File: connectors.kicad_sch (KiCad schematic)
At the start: 19 parts, among them J1 POWER_IN, J10 BUZZER, J11 SERVO, J2 Header_to_RPi, J3 Front panel, J4 DHT INT, J5 DEHUM, J6 FAN, J7 LIGHTSENSOR, J8 DHT EXT, J9 HEAT

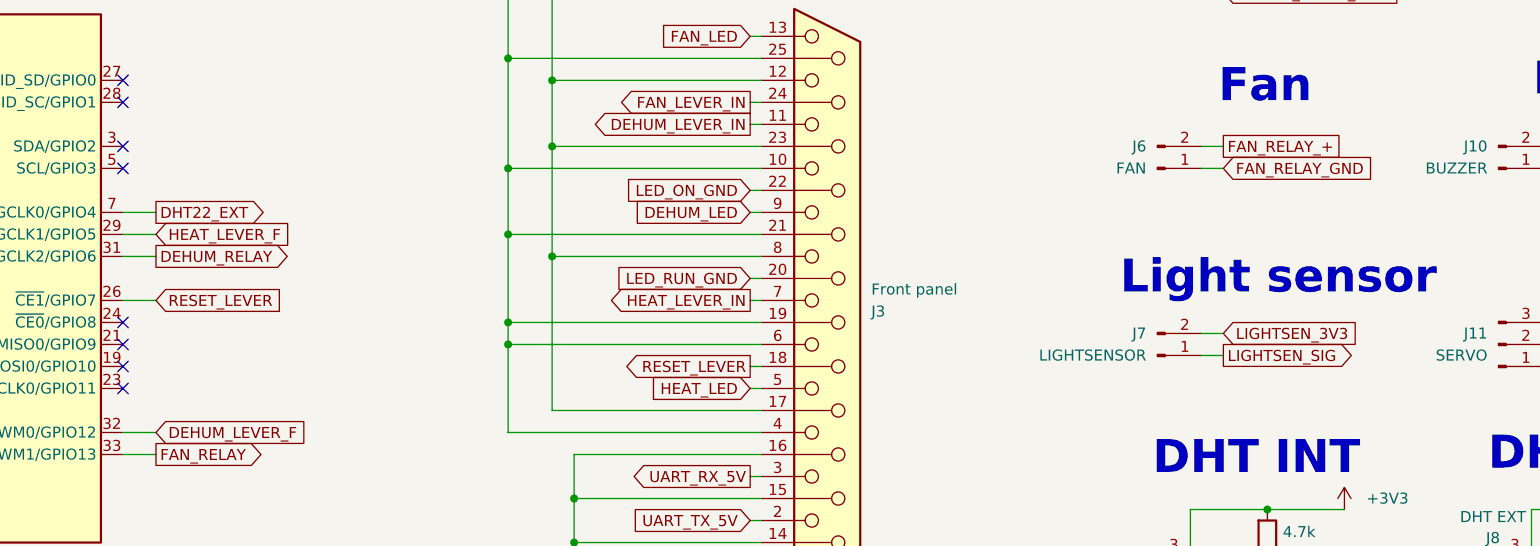
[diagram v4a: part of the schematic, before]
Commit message: Routing done, need to work on silkscreen
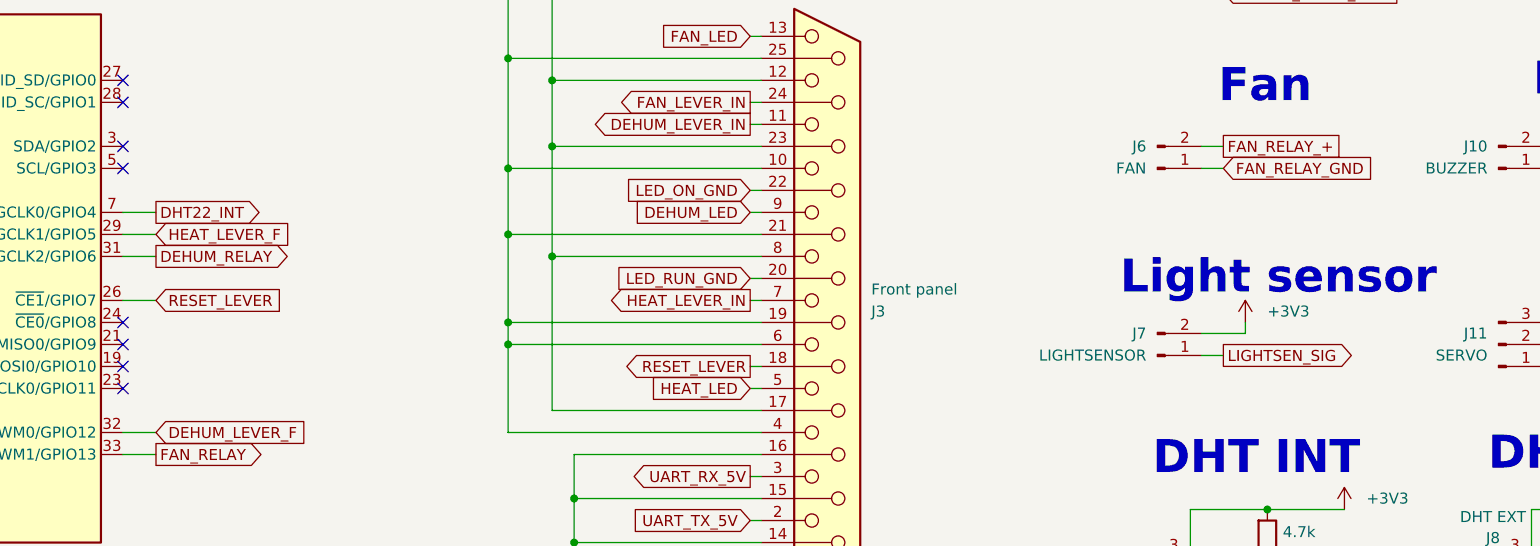
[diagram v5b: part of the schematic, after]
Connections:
- net LIGHTSEN_3V3 is gone; now on net +3V3: J7.2 (Pin_2)
- net DHT22_EXT: no longer J2.7 (GCLK0/GPIO4)
- net DHT22_INT: now also J2.7 (GCLK0/GPIO4)
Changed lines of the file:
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@@
 	(wire
 		(pts
+			(xy 220.98 71.12) (xy 215.9 71.12)
+		)
+		(stroke
+			(width 0)
+			(type default)
+		)
+	)
+	(wire
+		(pts
 			(xy 135.89 59.69) (xy 165.1 59.69)
 		)
@@
 	(wire
 		(pts
-			(xy 215.9 71.12) (xy 218.44 71.12)
-		)
-		(stroke
-			(width 0)
-			(type default)
-		)
-	)
-	(wire
-		(pts
 			(xy 76.2 30.48) (xy 76.2 31.75)
 		)
@@
 	(wire
 		(pts
+			(xy 220.98 69.85) (xy 220.98 71.12)
+		)
+		(stroke
+			(width 0)
+			(type default)
+		)
+	)
+	(wire
+		(pts
 			(xy 215.9 52.07) (xy 218.44 52.07)
 		)
@@
 		)
 	)
-	(global_label "LIGHTSEN_3V3"
-		(shape input)
-		(at 218.44 71.12 0)
-		(fields_autoplaced yes)
-		(effects
-			(font
-				(size 1.27 1.27)
-			)
-			(justify left)
-		)
-		(property "Intersheetrefs" "${INTERSHEET_REFS}"
-			(at 234.7904 71.12 0)
-			(effects
-				(font
-					(size 1.27 1.27)
-				)
-				(justify left)
-				(hide yes)
-			)
-		)
-	)
 	(global_label "DHT22_EXT"
 		(shape output)
@@
 		)
 	)
-	(global_label "DHT22_EXT"
+	(global_label "DHT22_INT"
 		(shape output)
 		(at 95.25 57.15 0)
@@
 		)
 		(property "Intersheetrefs" "${INTERSHEET_REFS}"
-			(at 108.516 57.15 0)
+			(at 108.0928 57.15 0)
 			(effects
 				(font
@@
 					(unit 1)
 				)
+			)
+		)
+	)
+	(symbol
+		(lib_id "power:+3V3")
+		(at 220.98 69.85 0)
+		(mirror y)
+		(unit 1)
+		(exclude_from_sim no)
+		(in_bom yes)
+		(on_board yes)
+		(dnp no)
+		(fields_autoplaced yes)
+		(property "Reference" "#PWR042"
+			(at 220.98 73.66 0)
+			(effects
+				(font
+					(size 1.27 1.27)
+				)
+				(hide yes)
+			)
+		)
+		(property "Value" "+3V3"
+			(at 223.52 68.5799 0)
+			(effects
+				(font
+					(size 1.27 1.27)
+				)
+				(justify right)
+			)
+		)
+		(property "Footprint" ""
+			(at 220.98 69.85 0)
+			(effects
+				(font
+					(size 1.27 1.27)
+				)
+				(hide yes)
+			)
+		)
+		(property "Datasheet" ""
+			(at 220.98 69.85 0)
+			(effects
+				(font
+					(size 1.27 1.27)
+				)
+				(hide yes)
+			)
+		)
+		(property "Description" "Power symbol creates a global label with name \"+3V3\""
+			(at 220.98 69.85 0)
+			(effects
+				(font
+					(size 1.27 1.27)
+				)
+				(hide yes)
+			)
+		)
+		(pin "1"
+		)
+		(instances
+			(project "ctahr_board"
+				(path "/dea08218-351b-4b2b-ab50-f60349a3e49f/ec8e726a-94a6-4011-a5bd-9e0cc5d57e5c"
+					(reference "#PWR042")
+					(unit 1)
+				)
